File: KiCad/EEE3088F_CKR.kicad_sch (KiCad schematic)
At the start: 0 parts

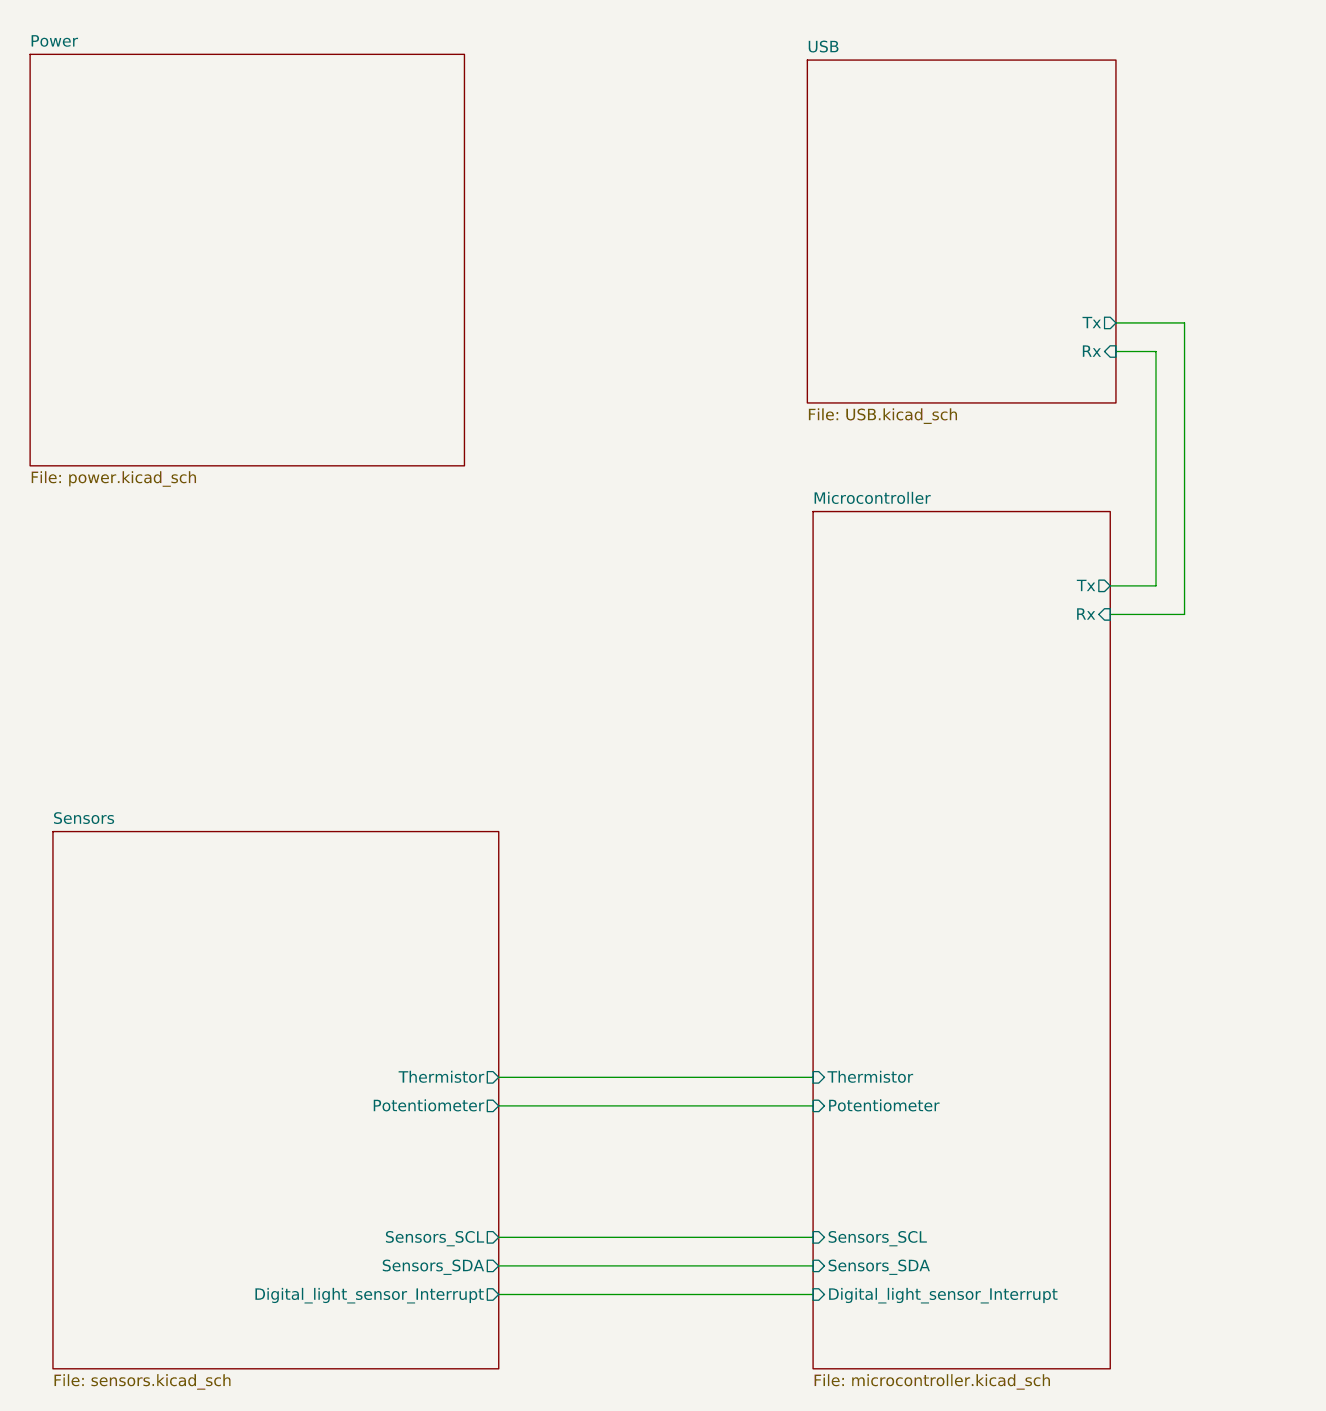
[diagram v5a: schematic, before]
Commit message: changed a bunch of net labels, changed some uc schem stuff
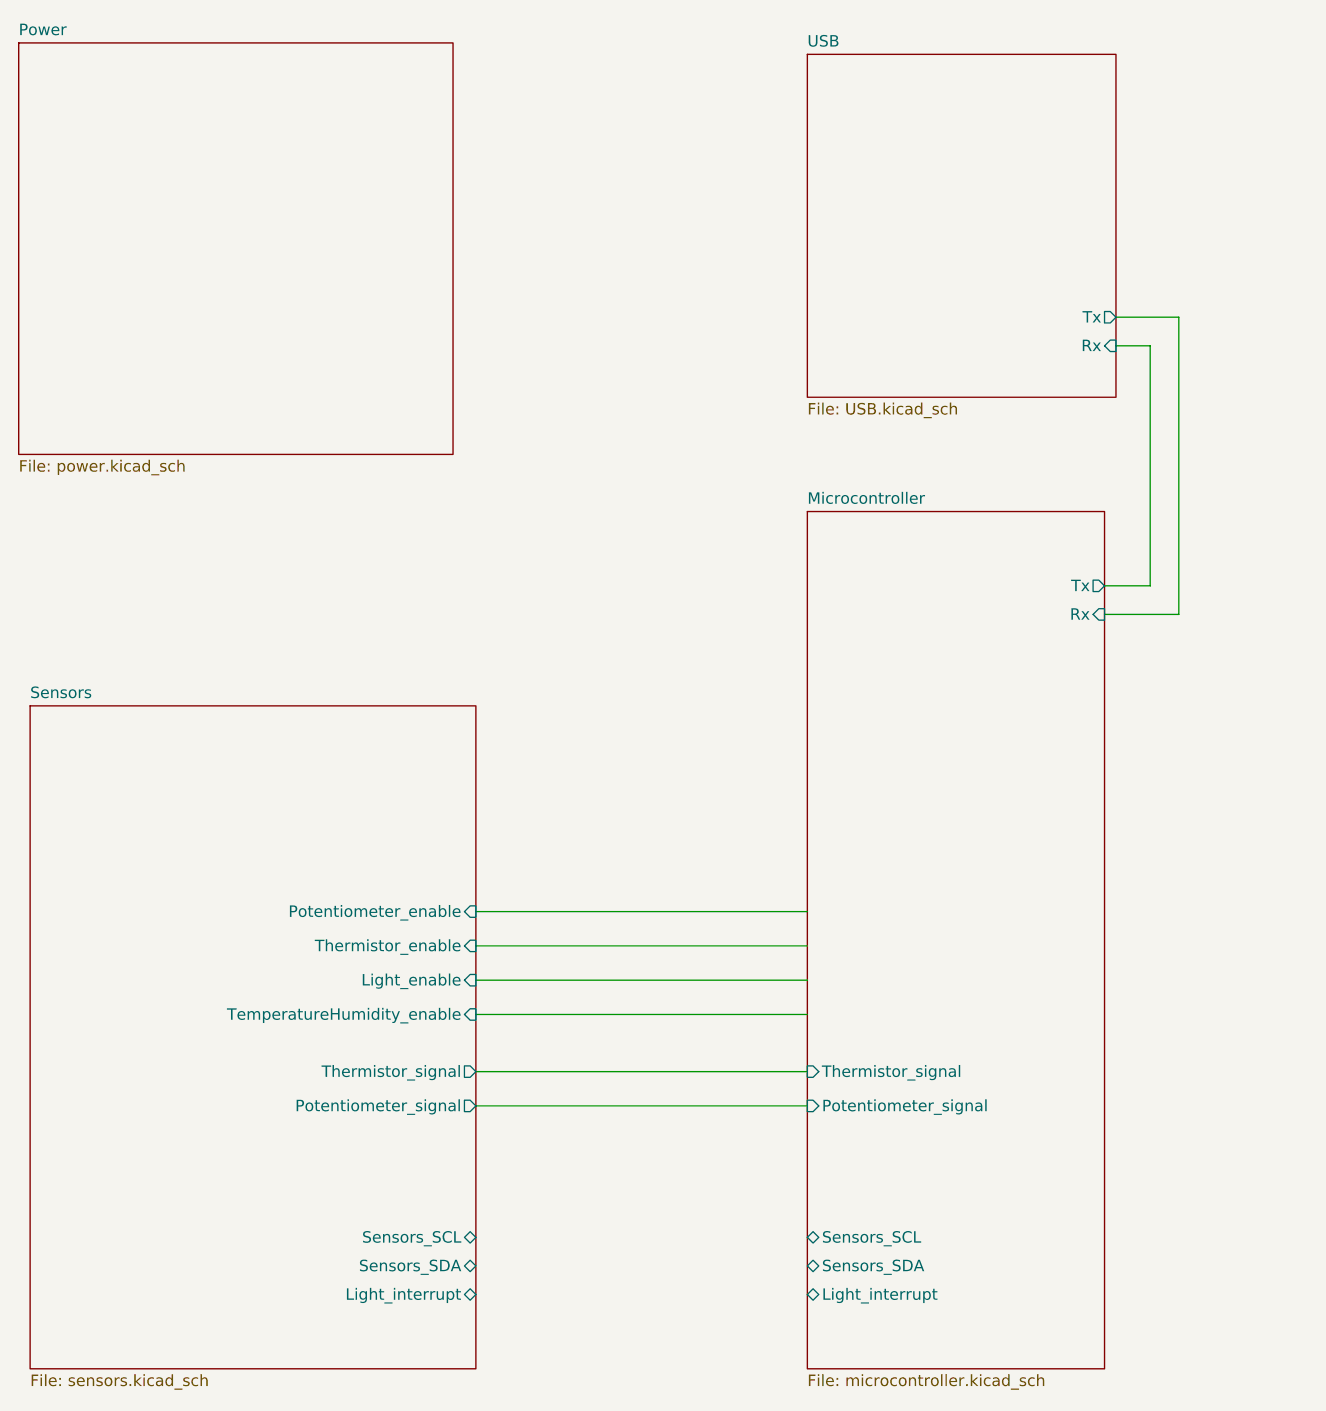
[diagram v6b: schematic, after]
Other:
- sheet Microcontroller ports: added Light_interrupt, Potentiometer_signal, Thermistor_signal; removed Digital_light_sensor_Interrupt, Potentiometer, Thermistor
- sheet Sensors ports: added Light_enable, Light_interrupt, Potentiometer_enable, Potentiometer_signal, TemperatureHumidity_enable, Thermistor_enable, Thermistor_signal; removed Digital_light_sensor_Interrupt, Potentiometer, Thermistor
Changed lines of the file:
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@@
     (title "Root")
     (date "2023-03-11")
-    (rev "v0.3")
+    (rev "v0.4")
     (company "UCT")
     (comment 1 "Authors: Cameron Clark, Robert Dugmore, Kian Frassek")
     (comment 2 "This is an overview sheet showing how the sub-circuits interconnect")
   )
-  (wire (pts (xy 156.845 86.995) (xy 151.765 86.995))
+  (wire (pts (xy 156.21 86.995) (xy 151.13 86.995))
     (stroke (width 0) (type default))
   )
-  (wire (pts (xy 83.82 141.605) (xy 118.745 141.605))
+  (wire (pts (xy 81.28 127) (xy 118.11 127))
     (stroke (width 0) (type default))
   )
-  (wire (pts (xy 83.82 162.56) (xy 118.745 162.56))
+  (wire (pts (xy 81.28 134.62) (xy 118.11 134.62))
     (stroke (width 0) (type default))
   )
-  (wire (pts (xy 83.82 159.385) (xy 118.745 159.385))
+  (wire (pts (xy 159.385 90.17) (xy 159.385 57.15))
     (stroke (width 0) (type default))
   )
-  (wire (pts (xy 160.02 90.17) (xy 160.02 57.785))
+  (wire (pts (xy 81.28 144.78) (xy 118.11 144.78))
     (stroke (width 0) (type default))
   )
-  (wire (pts (xy 83.82 144.78) (xy 118.745 144.78))
+  (wire (pts (xy 156.21 60.325) (xy 156.21 86.995))
     (stroke (width 0) (type default))
   )
-  (wire (pts (xy 156.845 60.96) (xy 156.845 86.995))
+  (wire (pts (xy 81.28 123.19) (xy 118.11 123.19))
     (stroke (width 0) (type default))
   )
-  (wire (pts (xy 152.4 60.96) (xy 156.845 60.96))
+  (wire (pts (xy 152.4 60.325) (xy 156.21 60.325))
     (stroke (width 0) (type default))
   )
-  (wire (pts (xy 160.02 57.785) (xy 152.4 57.785))
+  (wire (pts (xy 81.28 130.81) (xy 118.11 130.81))
     (stroke (width 0) (type default))
   )
-  (wire (pts (xy 151.765 90.17) (xy 160.02 90.17))
+  (wire (pts (xy 159.385 57.15) (xy 152.4 57.15))
     (stroke (width 0) (type default))
   )
-  (wire (pts (xy 83.82 165.735) (xy 118.745 165.735))
+  (wire (pts (xy 151.13 90.17) (xy 159.385 90.17))
     (stroke (width 0) (type default))
   )
-  (sheet (at 118.11 28.575) (size 34.29 38.1) (fields_autoplaced)
+  (wire (pts (xy 81.28 140.97) (xy 118.11 140.97))
+    (stroke (width 0) (type default))
+  )
+  (sheet (at 118.11 27.94) (size 34.29 38.1) (fields_autoplaced)
     (stroke (width 0.1524) (type solid))
     (fill (color 0 0 0 0.0000))
-    (property "Sheetname" "USB" (at 118.11 27.8634 0)
+    (property "Sheetname" "USB" (at 118.11 27.2284 0)
       (effects (font (size 1.27 1.27)) (justify left bottom))
     )
-    (property "Sheetfile" "USB.kicad_sch" (at 118.11 67.2596 0)
+    (property "Sheetfile" "USB.kicad_sch" (at 118.11 66.6246 0)
       (effects (font (size 1.27 1.27)) (justify left top))
     )
-    (pin "Tx" output (at 152.4 57.785 0)
+    (pin "Tx" output (at 152.4 57.15 0)
       (effects (font (size 1.27 1.27)) (justify right))
     )
-    (pin "Rx" input (at 152.4 60.96 0)
+    (pin "Rx" input (at 152.4 60.325 0)
       (effects (font (size 1.27 1.27)) (justify right))
     )
@@
     )
   )
-  (sheet (at 118.745 78.74) (size 33.02 95.25) (fields_autoplaced)
+  (sheet (at 118.11 78.74) (size 33.02 95.25) (fields_autoplaced)
     (stroke (width 0.1524) (type solid))
     (fill (color 0 0 0 0.0000))
-    (property "Sheetname" "Microcontroller" (at 118.745 78.0284 0)
+    (property "Sheetname" "Microcontroller" (at 118.11 78.0284 0)
       (effects (font (size 1.27 1.27)) (justify left bottom))
     )
-    (property "Sheetfile" "microcontroller.kicad_sch" (at 118.745 174.5746 0)
+    (property "Sheetfile" "microcontroller.kicad_sch" (at 118.11 174.5746 0)
       (effects (font (size 1.27 1.27)) (justify left top))
     )
-    (pin "Potentiometer" input (at 118.745 144.78 180)
+    (pin "Sensors_SCL" bidirectional (at 118.11 159.385 180)
       (effects (font (size 1.27 1.27)) (justify left))
     )
-    (pin "Thermistor" input (at 118.745 141.605 180)
+    (pin "Sensors_SDA" bidirectional (at 118.11 162.56 180)
       (effects (font (size 1.27 1.27)) (justify left))
     )
-    (pin "Sensors_SCL" input (at 118.745 159.385 180)
+    (pin "Light_interrupt" bidirectional (at 118.11 165.735 180)
       (effects (font (size 1.27 1.27)) (justify left))
     )
-    (pin "Sensors_SDA" input (at 118.745 162.56 180)
+    (pin "Rx" input (at 151.13 90.17 0)
+      (effects (font (size 1.27 1.27)) (justify right))
+    )
+    (pin "Tx" output (at 151.13 86.995 0)
+      (effects (font (size 1.27 1.27)) (justify right))
+    )
+    (pin "Thermistor_signal" input (at 118.11 140.97 180)
       (effects (font (size 1.27 1.27)) (justify left))
     )
-    (pin "Digital_light_sensor_Interrupt" input (at 118.745 165.735 180)
+    (pin "Potentiometer_signal" input (at 118.11 144.78 180)
       (effects (font (size 1.27 1.27)) (justify left))
-    )
-    (pin "Rx" input (at 151.765 90.17 0)
-      (effects (font (size 1.27 1.27)) (justify right))
-    )
-    (pin "Tx" output (at 151.765 86.995 0)
-      (effects (font (size 1.27 1.27)) (justify right))
     )
     (instances
@@
     )
   )
-  (sheet (at 31.75 27.94) (size 48.26 45.72) (fields_autoplaced)
+  (sheet (at 30.48 26.67) (size 48.26 45.72) (fields_autoplaced)
     (stroke (width 0.1524) (type solid))
     (fill (color 0 0 0 0.0000))
-    (property "Sheetname" "Power" (at 31.75 27.2284 0)
+    (property "Sheetname" "Power" (at 30.48 25.9584 0)
       (effects (font (size 1.27 1.27)) (justify left bottom))
     )
-    (property "Sheetfile" "power.kicad_sch" (at 31.75 74.2446 0)
+    (property "Sheetfile" "power.kicad_sch" (at 30.48 72.9746 0)
       (effects (font (size 1.27 1.27)) (justify left top))
     )
@@
     )
   )
-  (sheet (at 34.29 114.3) (size 49.53 59.69) (fields_autoplaced)
+  (sheet (at 31.75 100.33) (size 49.53 73.66) (fields_autoplaced)
     (stroke (width 0.1524) (type solid))
     (fill (color 0 0 0 0.0000))
-    (property "Sheetname" "Sensors" (at 34.29 113.5884 0)
+    (property "Sheetname" "Sensors" (at 31.75 99.6184 0)
       (effects (font (size 1.27 1.27)) (justify left bottom))
     )
-    (property "Sheetfile" "sensors.kicad_sch" (at 34.29 174.5746 0)
+    (property "Sheetfile" "sensors.kicad_sch" (at 31.75 174.5746 0)
       (effects (font (size 1.27 1.27)) (justify left top))
     )
-    (pin "Digital_light_sensor_Interrupt" output (at 83.82 165.735 0)
+    (pin "Light_interrupt" bidirectional (at 81.28 165.735 0)
       (effects (font (size 1.27 1.27)) (justify right))
     )
-    (pin "Sensors_SDA" output (at 83.82 162.56 0)
+    (pin "Sensors_SDA" bidirectional (at 81.28 162.56 0)
       (effects (font (size 1.27 1.27)) (justify right))
     )
-    (pin "Thermistor" output (at 83.82 141.605 0)
+    (pin "Thermistor_signal" output (at 81.28 140.97 0)
       (effects (font (size 1.27 1.27)) (justify right))
     )
-    (pin "Potentiometer" output (at 83.82 144.78 0)
+    (pin "Potentiometer_signal" output (at 81.28 144.78 0)
       (effects (font (size 1.27 1.27)) (justify right))
     )
-    (pin "Sensors_SCL" output (at 83.82 159.385 0)
+    (pin "Sensors_SCL" bidirectional (at 81.28 159.385 0)
       (effects (font (size 1.27 1.27)) (justify right))
     )
+    (pin "TemperatureHumidity_enable" input (at 81.28 134.62 0)
+      (effects (font (size 1.27 1.27)) (justify right))
+    )
+    (pin "Potentiometer_enable" input (at 81.28 123.19 0)
+      (effects (font (size 1.27 1.27)) (justify right))
+    )
+    (pin "Thermistor_enable" input (at 81.28 127 0)
+      (effects (font (size 1.27 1.27)) (justify right))
+    )
+    (pin "Light_enable" input (at 81.28 130.81 0)
+      (effects (font (size 1.27 1.27)) (justify right))
+    )
